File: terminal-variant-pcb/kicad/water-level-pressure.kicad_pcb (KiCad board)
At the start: 2 copper layers, 93.3 x 60.1 mm, 39 parts, among them J1 Conn_01x03, J2 Conn_01x04, J3 Conn_01x02, T1 TestPoint, T10 TestPoint, T11 TestPoint, T12 TestPoint, T13 TestPoint, T14 TestPoint, T15 TestPoint, T16 TestPoint, T17 TestPoint, T18 TestPoint, T19 TestPoint, T2 TestPoint, T20 TestPoint, T21 TestPoint, T22 TestPoint, T23 TestPoint, T24 TestPoint, T25 TestPoint, T26 TestPoint, T27 TestPoint, T28 TestPoint, T29 TestPoint, T3 TestPoint, T30 TestPoint, T4 TestPoint, T5 TestPoint, T6 TestPoint, T7 TestPoint, T8 TestPoint, T9 TestPoint

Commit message: Add terminal block for sensor and update price.
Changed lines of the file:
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@@
 				(font
 					(size 1.27 1.27)
+					(thickness 0.15)
 				)
 			)

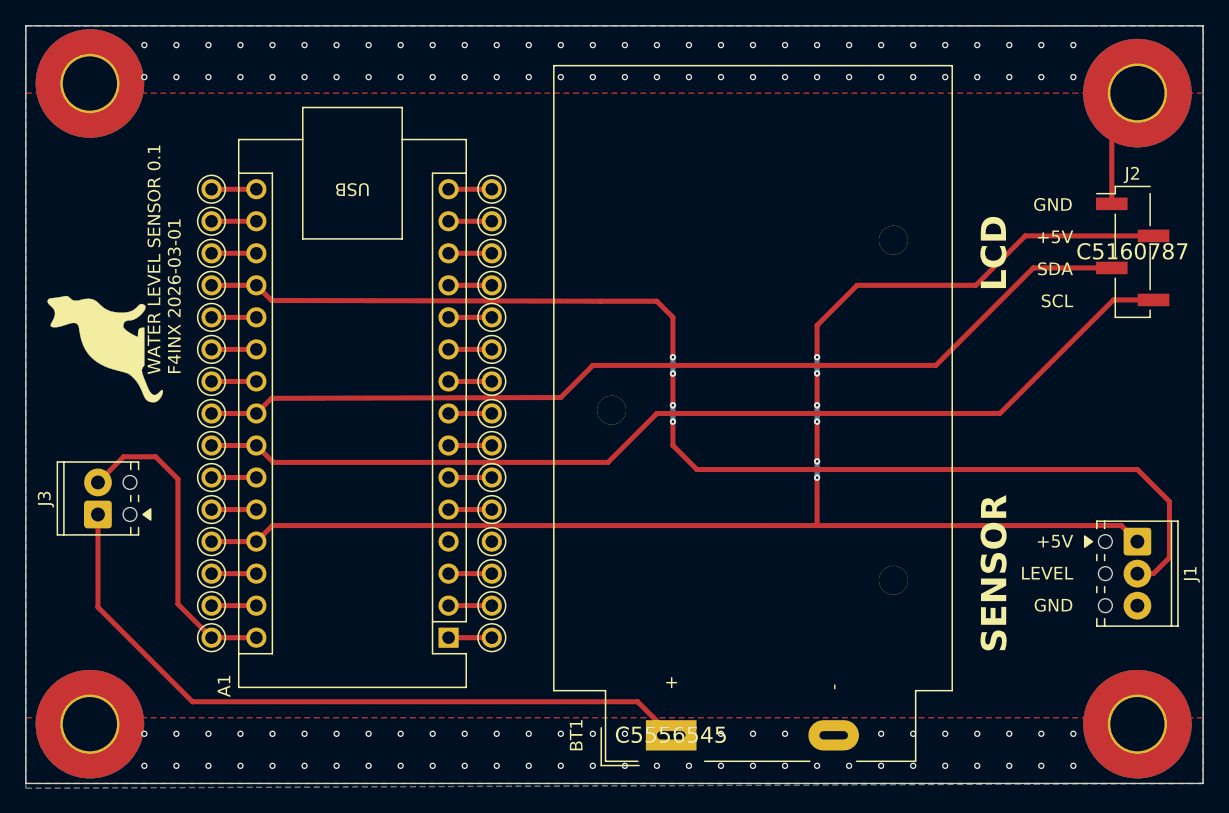
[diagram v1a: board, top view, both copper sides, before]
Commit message: Replacing Arduino footprint by pair of connectors footprints.
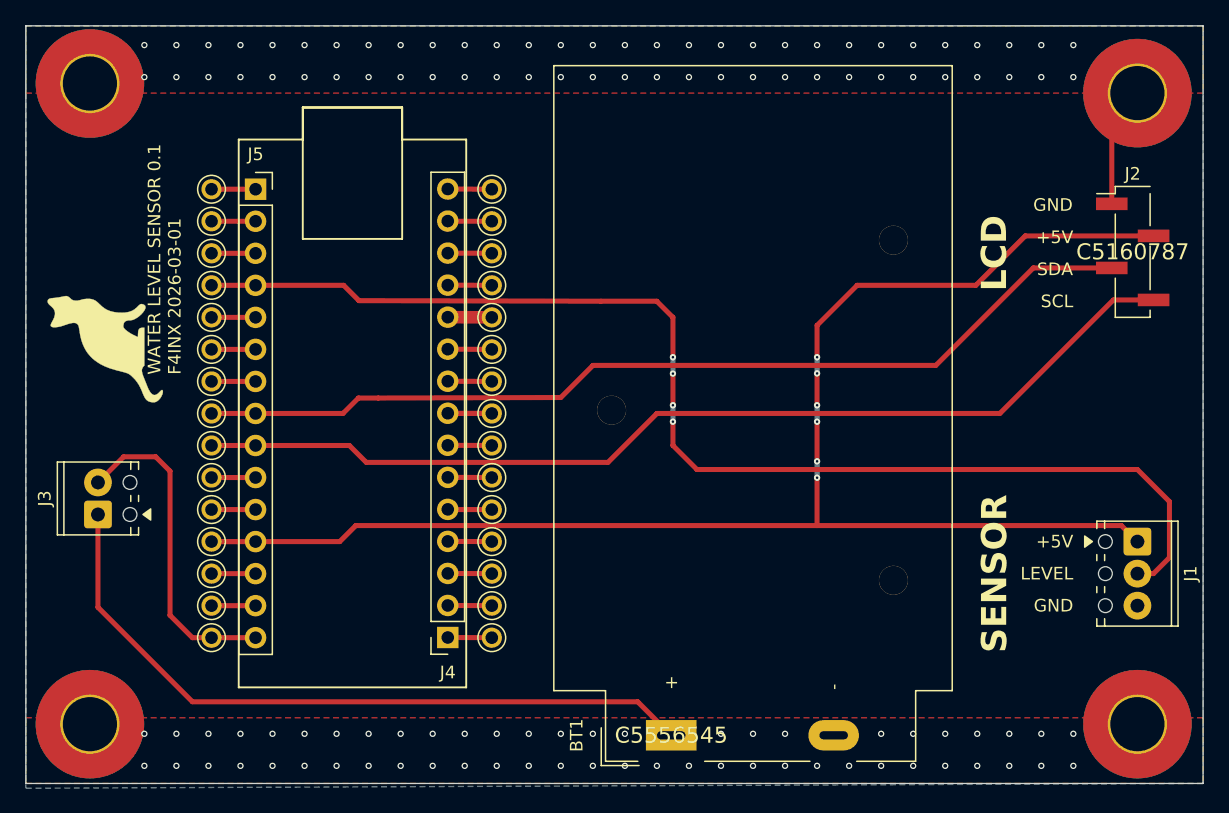
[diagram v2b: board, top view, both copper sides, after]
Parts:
- removed A1: Arduino_Nano_Every, Module:Arduino_Nano
- added J4: Conn_01x15_Socket, Connector_PinSocket_2.54mm:PinSocket_1x15_P2.54mm_Vertical, F.Cu at (150.3, 130.3)
- added J5: Conn_01x15_Socket, Connector_PinSocket_2.54mm:PinSocket_1x15_P2.54mm_Vertical, F.Cu at (135.1, 94.7)
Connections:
- T3 pad 1: Net-(A1-~{RESET}-Pad3) -> GND
- T4 pad 1: GND -> Net-(J4-Pin_4)
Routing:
- net Net-(J4-Pin_8): track 3.43 -> 6.92 mm
- net Net-(J4-Pin_4): track 0.00 -> 3.49 mm
- net GND: track 13.2 -> 16.6 mm
- net Net-(A1-~{RESET}-Pad3): track 3.43 -> 0.00 mm
- net +5V: track 120.0 -> 122.0 mm
- net /VIN: track 25.2 -> 26.0 mm

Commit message: Remove the only SMD component to avoid cost.
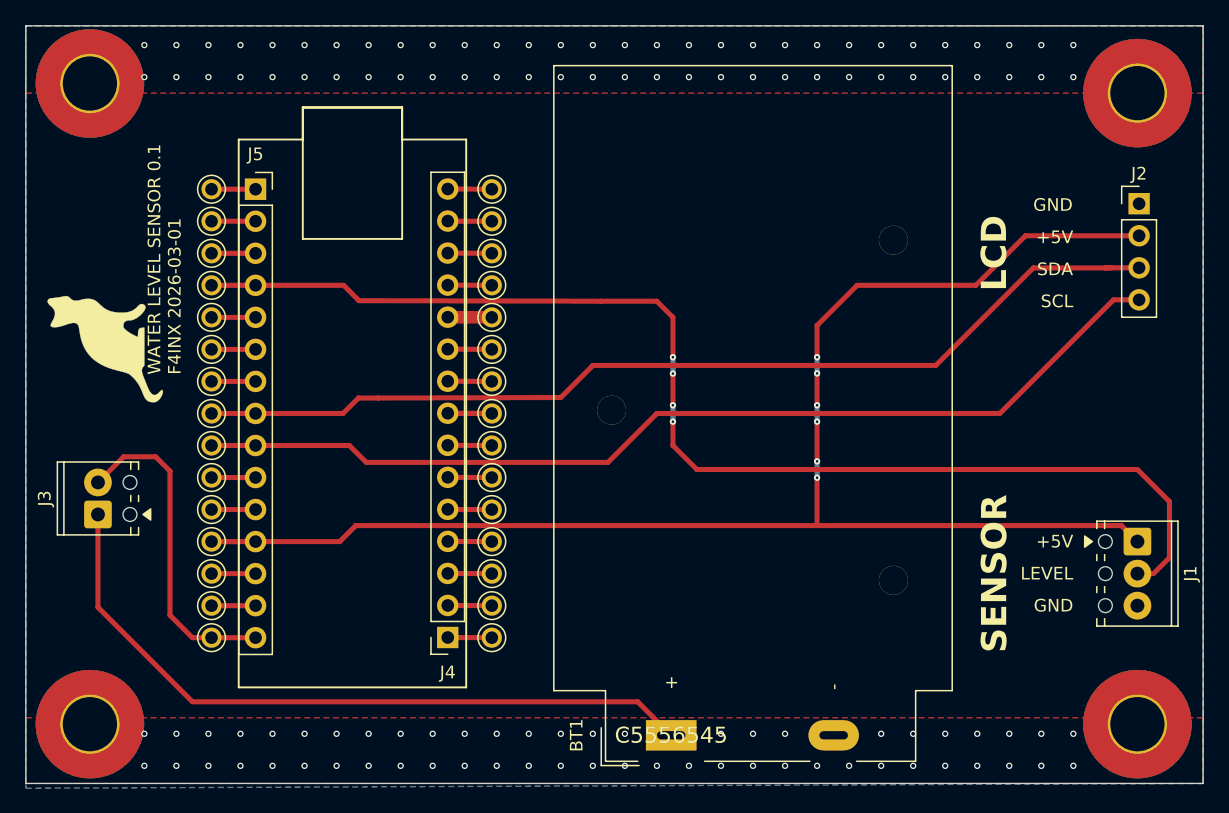
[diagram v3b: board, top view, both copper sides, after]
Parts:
- J2: footprint Connector_PinHeader_2.54mm:PinHeader_1x04_P2.54mm_Vertical_SMD_Pin1Left -> Connector_PinHeader_2.54mm:PinHeader_1x04_P2.54mm_Vertical
- moved J2 3.85 mm to (205.1, 95.9)
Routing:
- net GND: track 16.6 -> 10.0 mm
- net /SDA: track 76.1 -> 78.8 mm
- net +5V: track 122.0 -> 120.9 mm
- net /SCL: track 80.6 -> 79.4 mm

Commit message: Version 0.2 following Gönül Demir's review. Simplified routing without crossings. No trace between pads for clearance. Increase supplies thickness to 1 mm. Fix thickness of one of the Arduino to pads trace. Update version number and date. Update pcb and 3D pictures.
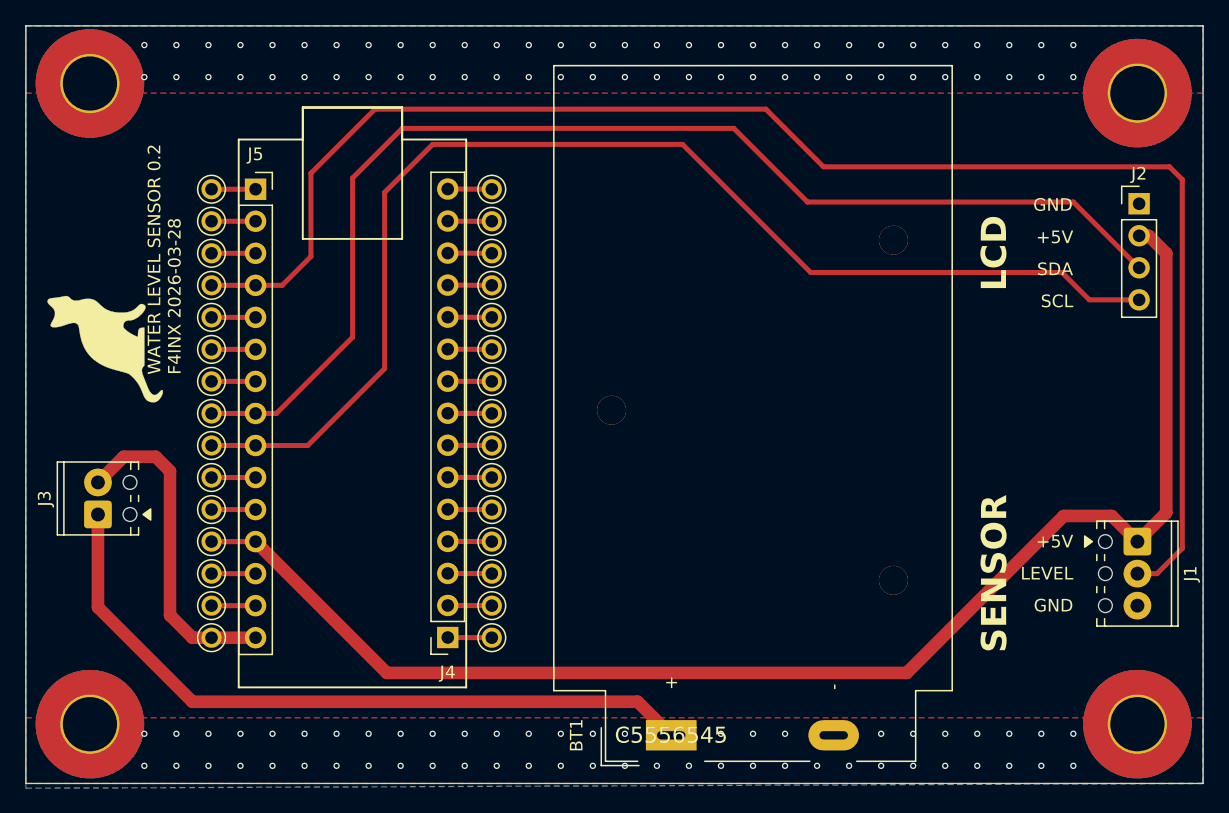
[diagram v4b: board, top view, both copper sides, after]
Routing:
- net /LEVEL: track 96.5 -> 122.6 mm, vias 4 -> 0
- net /SCL: track 79.4 -> 96.7 mm
- net /SDA: track 78.8 -> 94.9 mm
- net +5V: track 120.9 -> 112.3 mm, vias 6 -> 0
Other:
- board text added: "WATER LEVEL SENSOR 0.2 F4INX 2026-03-28"
- board text removed: "WATER LEVEL SENSOR 0.1 F4INX 2026-03-01"

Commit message: Version 0.3 following Gönül Demir's review. Fix thickness of 5V line between Arduino and pads. Route SDA and SCL together, in the same side of the hole.
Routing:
- net +5V: track 112.3 -> 110.3 mm
- net /SDA: track 94.9 -> 96.0 mm
- net /SCL: track 96.7 -> 97.2 mm
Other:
- board text added: "WATER LEVEL SENSOR 0.3 F4INX 2026-03-28"
- board text removed: "WATER LEVEL SENSOR 0.2 F4INX 2026-03-28"
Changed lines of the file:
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@@
 		)
 	)
-	(gr_text "WATER LEVEL SENSOR 0.2\nF4INX 2026-03-28"
+	(gr_text "WATER LEVEL SENSOR 0.3\nF4INX 2026-03-28"
 		(at 129.23297 109.451056 90)
 		(layer "F.SilkS")
@@
 	)
 	(segment
+		(start 146.685 89.916)
+		(end 142.748 93.853)
+		(width 0.4)
+		(layer "F.Cu")
+		(net "/SDA")
+	)
+	(segment
+		(start 142.748 93.853)
+		(end 142.748 106.4785)
+		(width 0.4)
+		(layer "F.Cu")
+		(net "/SDA")
+	)
+	(segment
+		(start 136.7045 112.522)
+		(end 131.562 112.522)
+		(width 0.4)
+		(layer "F.Cu")
+		(net "/SDA")
+	)
+	(segment
+		(start 202.049869 100.972131)
+		(end 200.66 102.362)
+		(width 0.4)
+		(layer "F.Cu")
+		(net "/SDA")
+	)
+	(segment
 		(start 142.748 106.4785)
-		(end 142.748 93.853)
-		(width 0.4)
-		(layer "F.Cu")
-		(net "/SDA")
-	)
-	(segment
-		(start 146.685 89.916)
-		(end 172.974 89.916)
-		(width 0.4)
-		(layer "F.Cu")
-		(net "/SDA")
-	)
-	(segment
-		(start 136.7045 112.522)
-		(end 142.748 106.4785)
-		(width 0.4)
-		(layer "F.Cu")
-		(net "/SDA")
-	)
-	(segment
-		(start 142.748 93.853)
+		(end 136.7045 112.522)
+		(width 0.4)
+		(layer "F.Cu")
+		(net "/SDA")
+	)
+	(segment
+		(start 205.110972 100.972131)
+		(end 202.049869 100.972131)
+		(width 0.4)
+		(layer "F.Cu")
+		(net "/SDA")
+	)
+	(segment
+		(start 178.816 102.362)
+		(end 166.37 89.916)
+		(width 0.4)
+		(layer "F.Cu")
+		(net "/SDA")
+	)
+	(segment
+		(start 200.66 102.362)
+		(end 178.816 102.362)
+		(width 0.4)
+		(layer "F.Cu")
+		(net "/SDA")
+	)
+	(segment
+		(start 166.37 89.916)
 		(end 146.685 89.916)
-		(width 0.4)
-		(layer "F.Cu")
-		(net "/SDA")
-	)
-	(segment
-		(start 199.896841 95.758)
-		(end 205.110972 100.972131)
-		(width 0.4)
-		(layer "F.Cu")
-		(net "/SDA")
-	)
-	(segment
-		(start 172.974 89.916)
-		(end 178.816 95.758)
-		(width 0.4)
-		(layer "F.Cu")
-		(net "/SDA")
-	)
-	(segment
-		(start 131.562 112.522)
-		(end 136.7045 112.522)
-		(width 0.4)
-		(layer "F.Cu")
-		(net "/SDA")
-	)
-	(segment
-		(start 178.816 95.758)
-		(end 199.896841 95.758)
 		(width 0.4)
 		(layer "F.Cu")
@@
 	)
 	(segment
-		(start 149.098 91.186)
-		(end 168.91 91.186)
+		(start 139.192 115.062)
+		(end 145.288 108.966)
+		(width 0.4)
+		(layer "F.Cu")
+		(net "/SCL")
+	)
+	(segment
+		(start 200.540131 104.902)
+		(end 201.93 103.512131)
+		(width 0.4)
+		(layer "F.Cu")
+		(net "/SCL")
+	)
+	(segment
+		(start 176.53 104.902)
+		(end 200.540131 104.902)
+		(width 0.4)
+		(layer "F.Cu")
+		(net "/SCL")
+	)
+	(segment
+		(start 145.288 94.996)
+		(end 148.336 91.948)
+		(width 0.4)
+		(layer "F.Cu")
+		(net "/SCL")
+	)
+	(segment
+		(start 201.93 103.512131)
+		(end 205.110972 103.512131)
+		(width 0.4)
+		(layer "F.Cu")
+		(net "/SCL")
+	)
+	(segment
+		(start 148.336 91.948)
+		(end 163.576 91.948)
+		(width 0.4)
+		(layer "F.Cu")
+		(net "/SCL")
+	)
+	(segment
+		(start 131.562 115.062)
+		(end 139.192 115.062)
 		(width 0.4)
 		(layer "F.Cu")
@@
 	)
 	(segment
-		(start 199.001869 101.346)
-		(end 201.168 103.512131)
-		(width 0.4)
-		(layer "F.Cu")
-		(net "/SCL")
-	)
-	(segment
-		(start 131.562 115.062)
-		(end 139.192 115.062)
-		(width 0.4)
-		(layer "F.Cu")
-		(net "/SCL")
-	)
-	(segment
-		(start 168.91 91.186)
-		(end 179.07 101.346)
-		(width 0.4)
-		(layer "F.Cu")
-		(net "/SCL")
-	)
-	(segment
-		(start 179.07 101.346)
-		(end 199.001869 101.346)
-		(width 0.4)
-		(layer "F.Cu")
-		(net "/SCL")
-	)
-	(segment
-		(start 139.192 115.062)
-		(end 145.288 108.966)
-		(width 0.4)
-		(layer "F.Cu")
-		(net "/SCL")
-	)
-	(segment
-		(start 145.288 94.996)
-		(end 149.098 91.186)
-		(width 0.4)
-		(layer "F.Cu")
-		(net "/SCL")
-	)
-	(segment
-		(start 201.168 103.512131)
-		(end 205.110972 103.512131)
+		(start 163.576 91.948)
+		(end 176.53 104.902)
 		(width 0.4)
 		(layer "F.Cu")
@@
 	)
 	(segment
-		(start 133.604 122.682)
-		(end 131.562 122.682)
-		(width 0.4)
-		(layer "F.Cu")
-		(net "+5V")
-	)
-	(segment
 		(start 207.264 120.396)
 		(end 204.978 122.682)
@@
 		(start 135.0545 122.682)
 		(end 131.562 122.682)
-		(width 0.4)
-		(layer "F.Cu")
-		(net "+5V")
+		(width 1)
+		(layer "F.Cu")
+		(net "+5V")

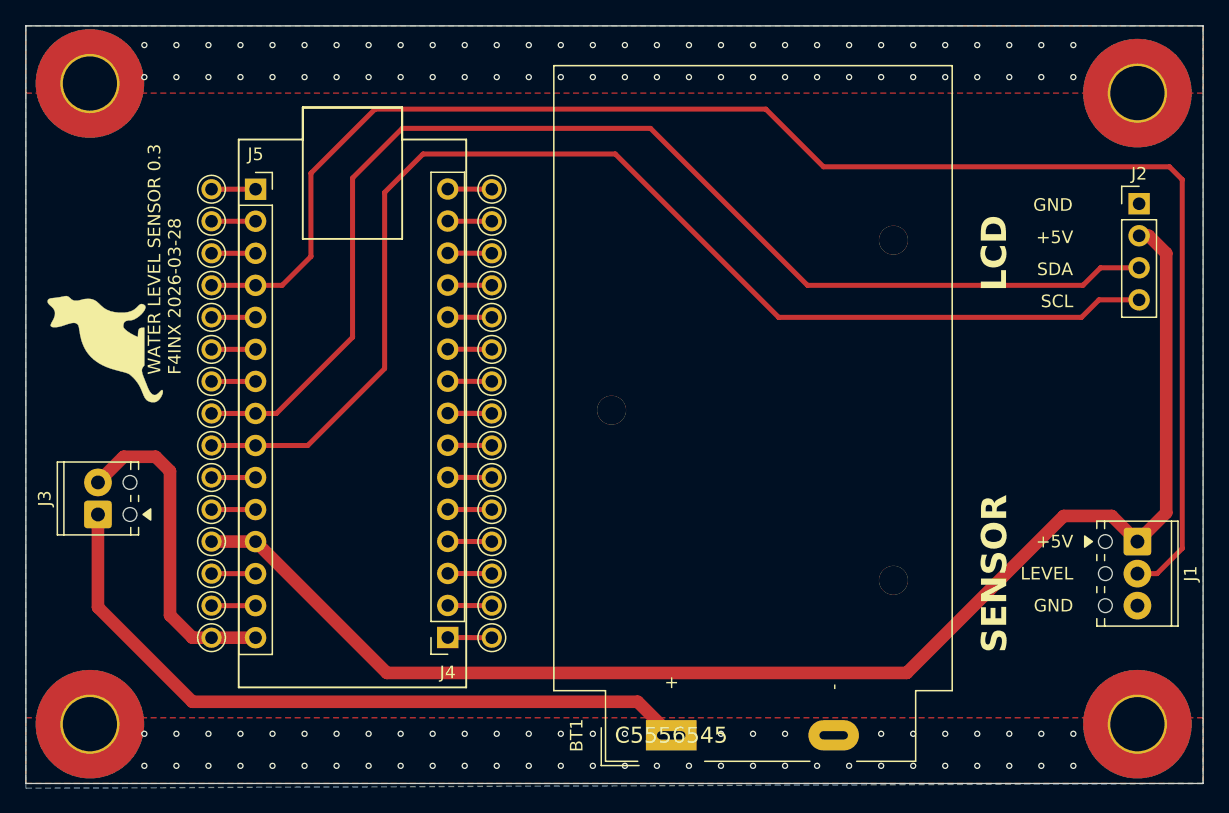
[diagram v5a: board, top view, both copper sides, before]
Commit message: Version 0.4. Slight ptimisation of 5V routing. 5V trace outside of silkscreen. LCD silkscreen outside of SDA trace. Raytracing for 3D view.
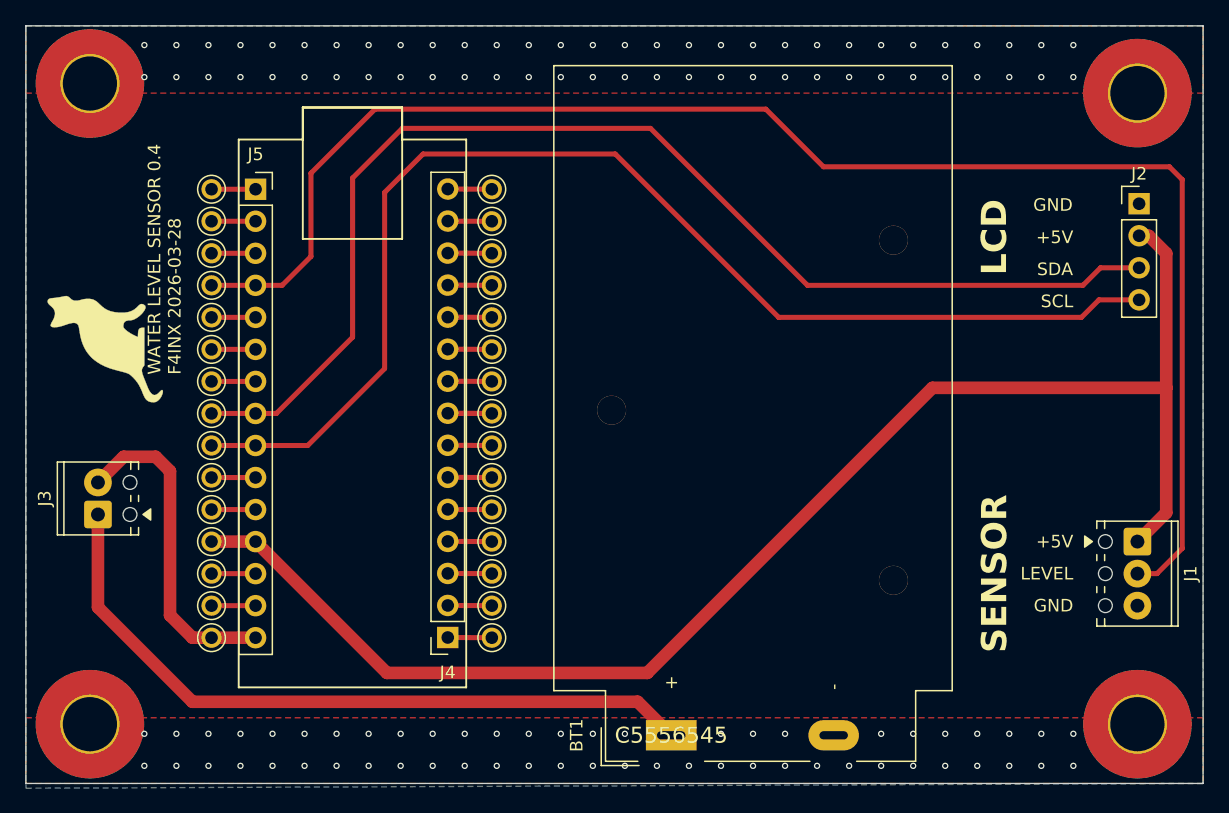
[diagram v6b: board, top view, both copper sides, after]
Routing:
- net +5V: track 110.3 -> 115.9 mm
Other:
- board text added: "WATER LEVEL SENSOR 0.4 F4INX 2026-03-28"
- board text removed: "WATER LEVEL SENSOR 0.3 F4INX 2026-03-28"
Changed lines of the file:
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@@
 		)
 	)
-	(gr_text "WATER LEVEL SENSOR 0.3\nF4INX 2026-03-28"
+	(gr_text "WATER LEVEL SENSOR 0.4\nF4INX 2026-03-28"
 		(at 129.23297 109.451056 90)
 		(layer "F.SilkS")
@@
 	)
 	(gr_text "LCD"
-		(at 194.80339 99.812581 90)
+		(at 194.80339 98.542581 90)
 		(layer "F.SilkS")
 		(effects
@@
 	)
 	(segment
-		(start 199.136 120.65)
-		(end 186.69 133.096)
-		(width 1)
-		(layer "F.Cu")
-		(net "+5V")
-	)
-	(segment
 		(start 205.110972 98.432131)
 		(end 205.874131 98.432131)
@@
 	)
 	(segment
+		(start 188.722 110.49)
+		(end 166.116 133.096)
+		(width 1)
+		(layer "F.Cu")
+		(net "+5V")
+	)
+	(segment
+		(start 207.264 110.49)
+		(end 188.722 110.49)
+		(width 1)
+		(layer "F.Cu")
+		(net "+5V")
+	)
+	(segment
+		(start 166.116 133.096)
+		(end 145.4685 133.096)
+		(width 1)
+		(layer "F.Cu")
+		(net "+5V")
+	)
+	(segment
 		(start 207.264 99.822)
-		(end 207.264 120.396)
+		(end 207.264 110.49)
 		(width 1)
 		(layer "F.Cu")
@@
 	)
 	(segment
-		(start 202.946 120.65)
-		(end 199.136 120.65)
-		(width 1)
-		(layer "F.Cu")
-		(net "+5V")
-	)
-	(segment
-		(start 204.978 122.682)
-		(end 202.946 120.65)
+		(start 207.264 110.49)
+		(end 207.264 120.396)
 		(width 1)
 		(layer "F.Cu")
@@
 		(width 1)
 		(layer "F.Cu")
-		(net "+5V")
-	)
-	(segment
-		(start 186.69 133.096)
-		(end 145.4685 133.096)
-		(width 1)
-		(layer "F.Cu")
